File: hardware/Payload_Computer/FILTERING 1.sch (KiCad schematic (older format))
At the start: 3 parts

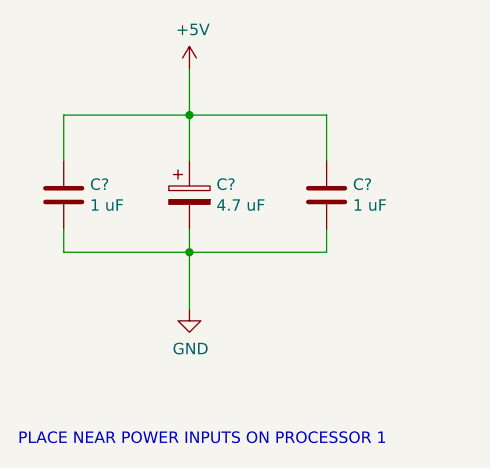
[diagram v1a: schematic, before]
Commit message: Finished BNO055
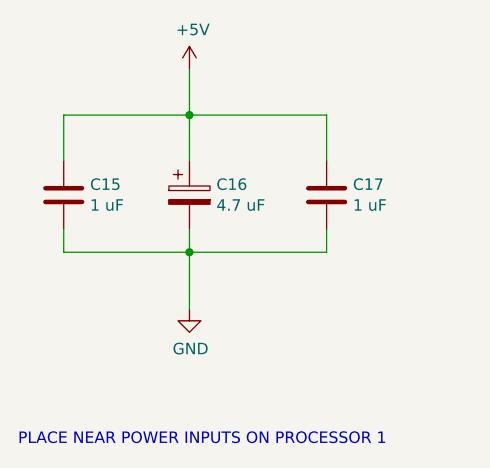
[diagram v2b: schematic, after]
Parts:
- gave numbers to parts that had none: 3
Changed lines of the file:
@@
 $Descr A4 11693 8268
 encoding utf-8
-Sheet 12 17
+Sheet 12 15
 Title ""
 Date ""
@@
 $EndDescr
 $Comp
-L Device:C C?
+L Device:C C15
 U 1 1 5F9946CA
 P 5250 4000
-F 0 "C?" H 5365 4046 50  0000 L CNN
+F 0 "C15" H 5365 4046 50  0000 L CNN
 F 1 "1 uF" H 5365 3955 50  0000 L CNN
 F 2 "" H 5288 3850 50  0001 C CNN
@@
 $EndComp
 $Comp
-L Device:C C?
+L Device:C C17
 U 1 1 5F9949A9
 P 6400 4000
-F 0 "C?" H 6515 4046 50  0000 L CNN
+F 0 "C17" H 6515 4046 50  0000 L CNN
 F 1 "1 uF" H 6515 3955 50  0000 L CNN
 F 2 "" H 6438 3850 50  0001 C CNN
@@
 $EndComp
 $Comp
-L Device:CP C?
+L Device:CP C16
 U 1 1 5F994B77
 P 5800 4000
-F 0 "C?" H 5918 4046 50  0000 L CNN
+F 0 "C16" H 5918 4046 50  0000 L CNN
 F 1 "4.7 uF" H 5918 3955 50  0000 L CNN
 F 2 "" H 5838 3850 50  0001 C CNN
@@
 $EndComp
 $Comp
-L power:+5V #PWR?
+L power:+5V #PWR0139
 U 1 1 5F994DD2
 P 5800 3450
-F 0 "#PWR?" H 5800 3300 50  0001 C CNN
+F 0 "#PWR0139" H 5800 3300 50  0001 C CNN
 F 1 "+5V" H 5815 3623 50  0000 C CNN
 F 2 "" H 5800 3450 50  0001 C CNN
@@
 $EndComp
 $Comp
-L power:GND #PWR?
+L power:GND #PWR0140
 U 1 1 5F995094
 P 5800 4500
-F 0 "#PWR?" H 5800 4250 50  0001 C CNN
+F 0 "#PWR0140" H 5800 4250 50  0001 C CNN
 F 1 "GND" H 5805 4327 50  0000 C CNN
 F 2 "" H 5800 4500 50  0001 C CNN
